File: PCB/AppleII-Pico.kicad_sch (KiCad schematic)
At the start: 29 parts, among them J1 Apple II, J2 DB15_Female_HighDensity_Mount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, J3 NOPAL, J4 Conn_02x08_Odd_Even, U1 74LCX16245, U2 74LCX16245, U5 PALCE16V8H-5JC/5, U6 Pi PICO, U7 AZ1117-3.3

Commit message: Better RPi Pico footprint
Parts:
- U6: footprint Package_DIP:DIP-40_W16.51mm_SMDSocket_LongPads -> MCU_RaspberryPi_and_Boards:RPi_Pico_SMD_TH
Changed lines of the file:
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@@
     (property "Reference" "U6" (id 0) (at 110.49 17.3482 0))
     (property "Value" "Pi PICO" (id 1) (at 110.49 19.6596 0))
-    (property "Footprint" "Package_DIP:DIP-40_W16.51mm_SMDSocket_LongPads" (id 2) (at 109.22 45.72 0)
+    (property "Footprint" "MCU_RaspberryPi_and_Boards:RPi_Pico_SMD_TH" (id 2) (at 109.22 45.72 0)
       (effects (font (size 1.27 1.27)) hide)
     )
@@
     )
     (path "/00000000-0000-0000-0000-000063a68952"
-      (reference "U6") (unit 1) (value "Pi PICO") (footprint "Package_DIP:DIP-40_W16.51mm_SMDSocket_LongPads")
+      (reference "U6") (unit 1) (value "Pi PICO") (footprint "MCU_RaspberryPi_and_Boards:RPi_Pico_SMD_TH")
     )
     (path "/00000000-0000-0000-0000-00006698c94f"

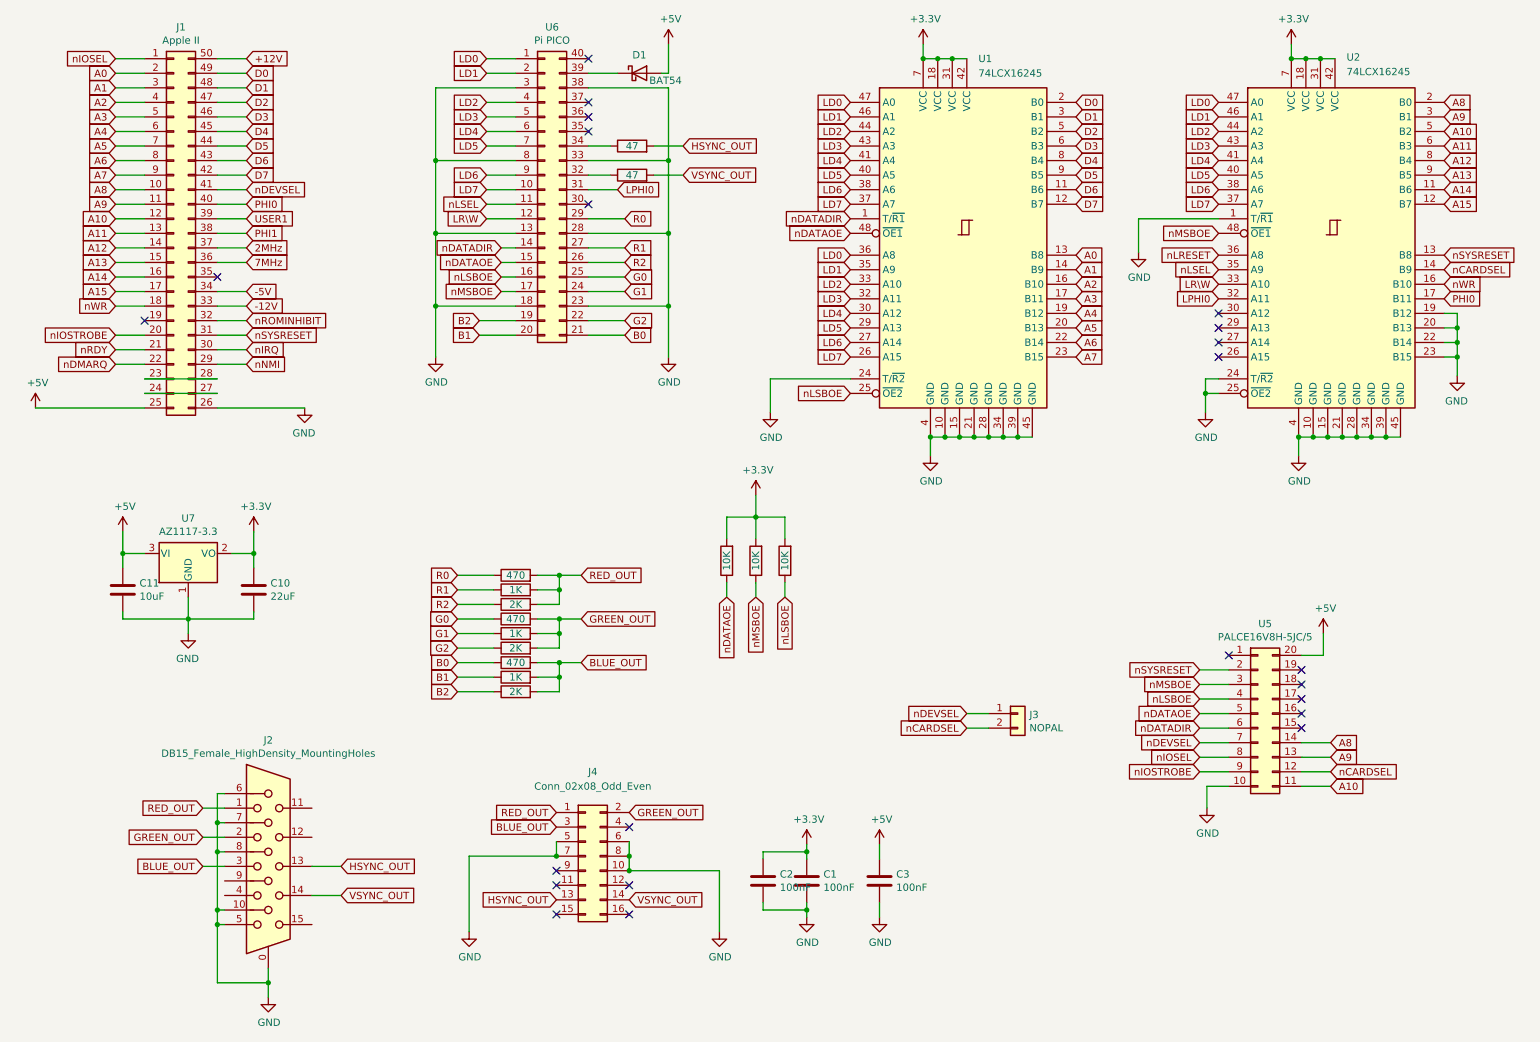
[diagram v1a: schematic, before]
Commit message: incorporate feedback
 - Pico W antenna cutout
 - Pico RUN button
 - Break-away HD15A connector
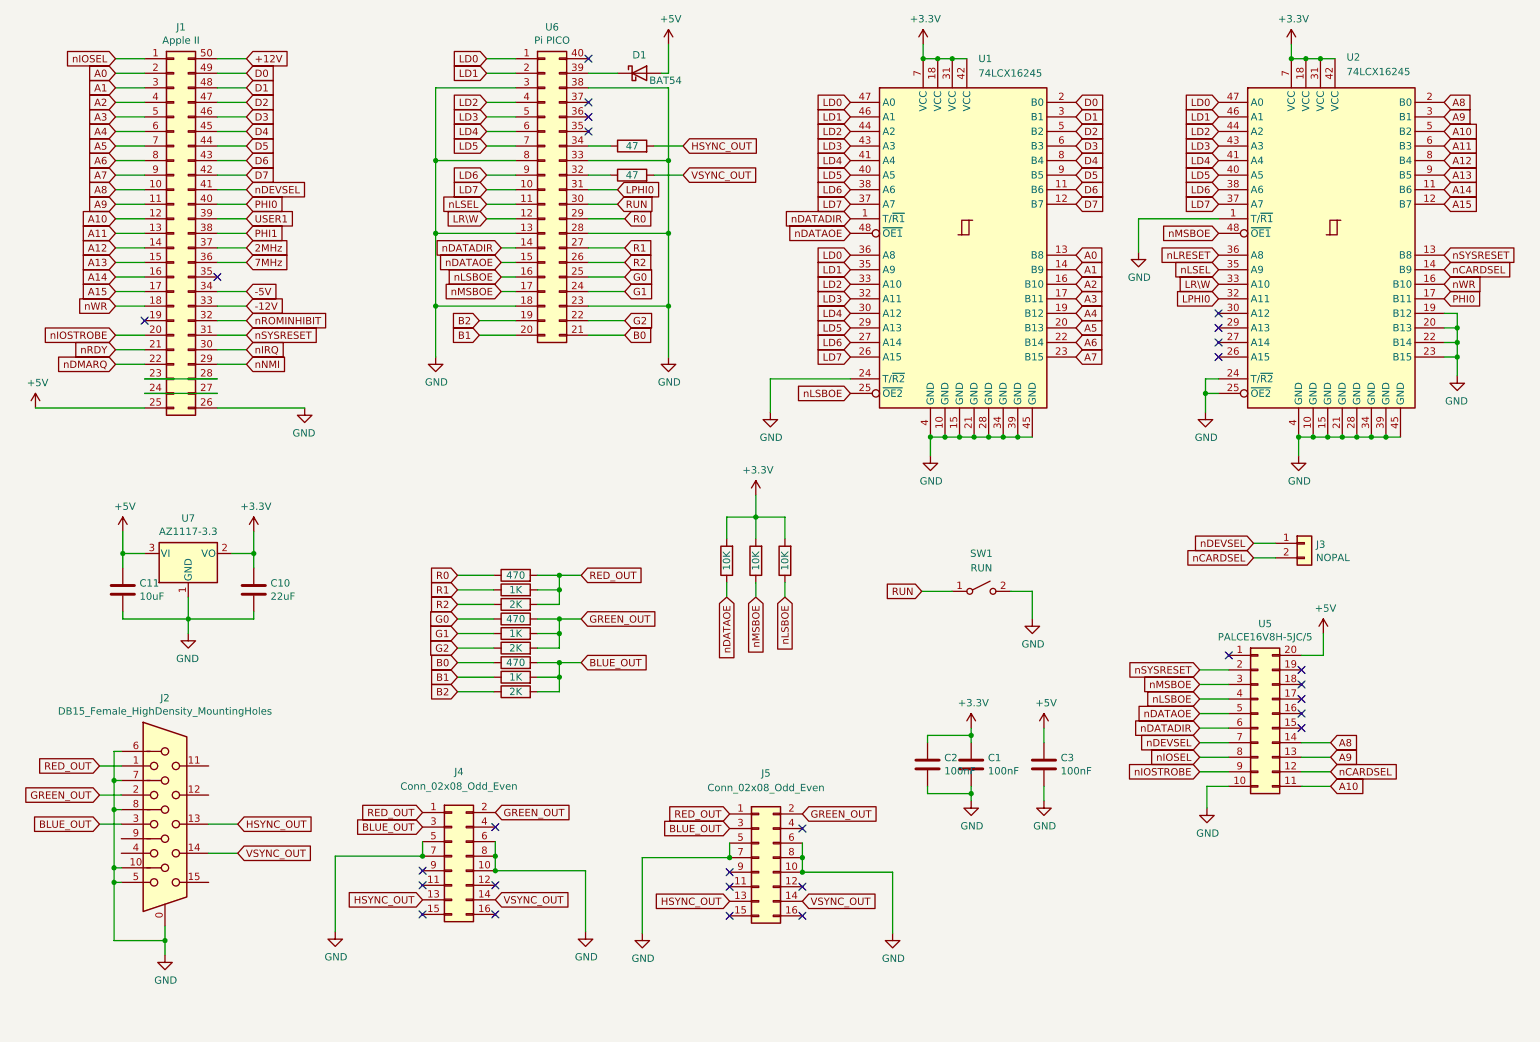
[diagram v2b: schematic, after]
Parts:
- added J5: Conn_02x08_Odd_Even, Connector_PinHeader_2.54mm:PinHeader_2x08_P2.54mm_Vertical, symbol Connector_Generic:Conn_02x08_Odd_Even
- added SW1: RUN, Button_Switch_SMD:SW_Push_1P1T_NO_6x6mm_H9.5mm, symbol Switch:SW_SPST
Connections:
- net BLUE_OUT: now also J5.3 (Pin_3)
- net GND: now also J5.10 (Pin_10), J5.5 (Pin_5), J5.6 (Pin_6), J5.7 (Pin_7), J5.8 (Pin_8), SW1.2 (B)
- net GREEN_OUT: now also J5.2 (Pin_2)
- net HSYNC_OUT: now also J5.13 (Pin_13)
- net RED_OUT: now also J5.1 (Pin_1)
- net VSYNC_OUT: now also J5.14 (Pin_14)
- net RUN: now reaches U6.30 (Pin_30)
- net RUN: now also SW1.1 (A)
- no-connect marks 23 -> 28
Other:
- moved on the sheet: C1, C2, C3, J2, J3, J4

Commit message: RUN => Pico Reset
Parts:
- SW1: value RUN -> Pico Reset
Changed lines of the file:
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@@
     (in_bom yes) (on_board yes)
     (property "Reference" "SW1" (id 0) (at 185.42 109.22 0))
-    (property "Value" "RUN" (id 1) (at 185.42 111.76 0))
+    (property "Value" "Pico Reset" (id 1) (at 185.42 111.76 0))
     (property "Footprint" "Button_Switch_SMD:SW_Push_1P1T_NO_6x6mm_H9.5mm" (id 2) (at 185.42 115.824 0)
       (effects (font (size 1.27 1.27)) hide)
@@
     )
     (path "/c1078c71-8ecb-4416-b362-632bf351b877"
-      (reference "SW1") (unit 1) (value "RUN") (footprint "Button_Switch_SMD:SW_Push_1P1T_NO_6x6mm_H9.5mm")
+      (reference "SW1") (unit 1) (value "Pico Reset") (footprint "Button_Switch_SMD:SW_Push_1P1T_NO_6x6mm_H9.5mm")
     )
     (path "/c189b8bd-871a-49df-bd93-46ab30fbe2a1"

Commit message: Fix TSSOP-48 footprint and move NOPAL
 - Use correct footprint for the TSSOP-48 case (closes #2)
 - Rename NOPAL to NOGAL and move it into the GAL footprint (closes #3)
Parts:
- J3: value NOPAL -> NOGAL
- U1: footprint Package_SO:TSSOP-48_8x12.5mm_P0.5mm -> Package_SO:TSSOP-48_6.1x9.7mm_P0.4mm
- U2: footprint Package_SO:TSSOP-48_8x12.5mm_P0.5mm -> Package_SO:TSSOP-48_6.1x12.5mm_P0.5mm
- U5: value PALCE16V8H-5JC/5 -> GAL16V8
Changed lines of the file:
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@@
     )
   )
-  (global_label "nCARDSEL" (shape input) (at 246.38 147.32 0) (fields_autoplaced)
-    (effects (font (size 1.27 1.27)) (justify left))
-    (property "Intersheet References" "${INTERSHEET_REFS}" (id 0) (at 0 0 0)
-      (effects (font (size 1.27 1.27)) hide)
+  (global_label "nCARDSEL" (shape output) (at 246.38 147.32 0) (fields_autoplaced)
+    (effects (font (size 1.27 1.27)) (justify left))
+    (property "Intersheet References" "${INTERSHEET_REFS}" (id 0) (at 258.1385 147.2406 0)
+      (effects (font (size 1.27 1.27)) (justify left) hide)
     )
   )
@@
       (effects (font (size 1.27 1.27)) (justify left))
     )
-    (property "Value" "NOPAL" (id 1) (at 243.84 109.9566 0)
+    (property "Value" "NOGAL" (id 1) (at 243.84 109.9566 0)
       (effects (font (size 1.27 1.27)) (justify left))
     )
@@
     (in_bom yes) (on_board yes)
     (property "Reference" "U5" (id 0) (at 234.95 121.4882 0))
-    (property "Value" "PALCE16V8H-5JC/5" (id 1) (at 234.95 123.7996 0))
+    (property "Value" "GAL16V8" (id 1) (at 234.95 123.7996 0))
     (property "Footprint" "Package_LCC:PLCC-20" (id 2) (at 233.68 137.16 0)
       (effects (font (size 1.27 1.27)) hide)
@@
       (effects (font (size 1.27 1.27)) (justify left))
     )
-    (property "Footprint" "Package_SO:TSSOP-48_8x12.5mm_P0.5mm" (id 2) (at 207.264 21.336 0)
+    (property "Footprint" "Package_SO:TSSOP-48_6.1x9.7mm_P0.4mm" (id 2) (at 207.264 21.336 0)
       (effects (font (size 1.27 1.27)) hide)
     )
@@
       (effects (font (size 1.27 1.27)) (justify left))
     )
-    (property "Footprint" "Package_SO:TSSOP-48_8x12.5mm_P0.5mm" (id 2) (at 271.526 21.336 0)
+    (property "Footprint" "Package_SO:TSSOP-48_6.1x12.5mm_P0.5mm" (id 2) (at 271.526 21.336 0)
       (effects (font (size 1.27 1.27)) hide)
     )
@@
     )
     (path "/00000000-0000-0000-0000-000063a3190c"
-      (reference "J3") (unit 1) (value "NOPAL") (footprint "Jumper:SolderJumper-2_P1.3mm_Open_TrianglePad1.0x1.5mm")
+      (reference "J3") (unit 1) (value "NOGAL") (footprint "Jumper:SolderJumper-2_P1.3mm_Open_TrianglePad1.0x1.5mm")
     )
     (path "/40c1df59-d376-490e-82b7-b056f34f1afc"
@@
     )
     (path "/c189b8bd-871a-49df-bd93-46ab30fbe2a1"
-      (reference "U1") (unit 1) (value "74LCX16245") (footprint "Package_SO:TSSOP-48_8x12.5mm_P0.5mm")
+      (reference "U1") (unit 1) (value "74LCX16245") (footprint "Package_SO:TSSOP-48_6.1x9.7mm_P0.4mm")
     )
     (path "/da52514b-32f6-46c0-9351-0f5bbc5d8c8f"
-      (reference "U2") (unit 1) (value "74LCX16245") (footprint "Package_SO:TSSOP-48_8x12.5mm_P0.5mm")
+      (reference "U2") (unit 1) (value "74LCX16245") (footprint "Package_SO:TSSOP-48_6.1x12.5mm_P0.5mm")
     )
     (path "/00000000-0000-0000-0000-000066540aaf"
-      (reference "U5") (unit 1) (value "PALCE16V8H-5JC/5") (footprint "Package_LCC:PLCC-20")
+      (reference "U5") (unit 1) (value "GAL16V8") (footprint "Package_LCC:PLCC-20")
     )
     (path "/00000000-0000-0000-0000-000063a68952"

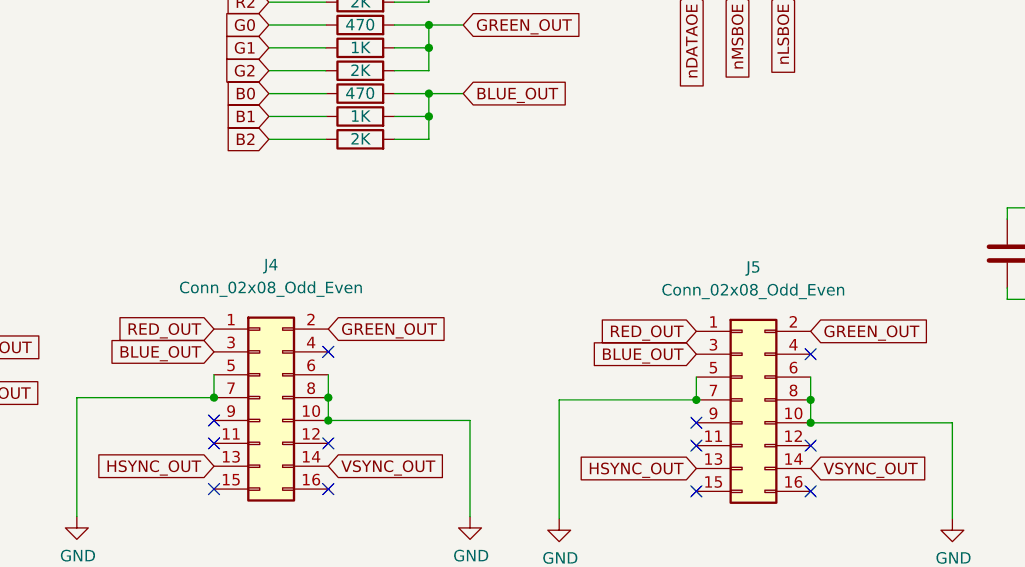
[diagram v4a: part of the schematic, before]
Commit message: silkscreen tweaks
closes #4
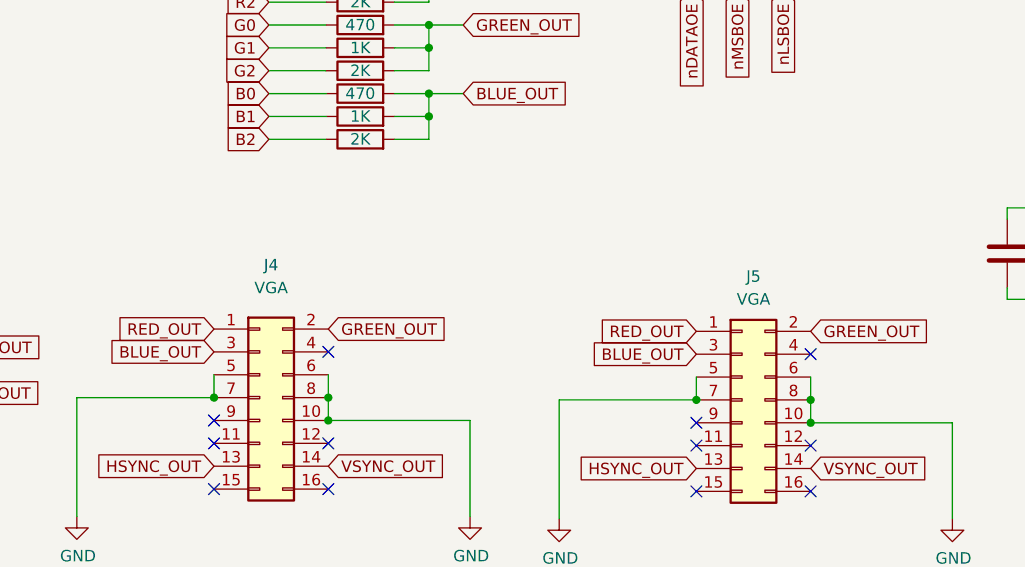
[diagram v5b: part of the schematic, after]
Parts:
- J4, J5: value Conn_02x08_Odd_Even -> VGA
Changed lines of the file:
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@@
     (in_bom yes) (on_board yes) (fields_autoplaced)
     (property "Reference" "J4" (id 0) (at 94.234 147.32 0))
-    (property "Value" "Conn_02x08_Odd_Even" (id 1) (at 94.234 149.86 0))
+    (property "Value" "VGA" (id 1) (at 94.234 149.86 0))
     (property "Footprint" "Connector_PinHeader_2.54mm:PinHeader_2x08_P2.54mm_Vertical" (id 2) (at 92.964 162.052 0)
       (effects (font (size 1.27 1.27)) hide)
@@
   (symbol (lib_id "Connector_Generic:Conn_02x08_Odd_Even") (at 146.558 162.306 0) (unit 1)
     (in_bom yes) (on_board yes) (fields_autoplaced)
-    (property "Reference" "J5" (id 0) (at 147.828 147.574 0))
-    (property "Value" "Conn_02x08_Odd_Even" (id 1) (at 147.828 150.114 0))
+    (property "Reference" "J5" (id 0) (at 147.828 148.59 0))
+    (property "Value" "VGA" (id 1) (at 147.828 151.13 0))
     (property "Footprint" "Connector_PinHeader_2.54mm:PinHeader_2x08_P2.54mm_Vertical" (id 2) (at 146.558 162.306 0)
       (effects (font (size 1.27 1.27)) hide)
@@
     )
     (path "/40c1df59-d376-490e-82b7-b056f34f1afc"
-      (reference "J4") (unit 1) (value "Conn_02x08_Odd_Even") (footprint "Connector_PinHeader_2.54mm:PinHeader_2x08_P2.54mm_Vertical")
+      (reference "J4") (unit 1) (value "VGA") (footprint "Connector_PinHeader_2.54mm:PinHeader_2x08_P2.54mm_Vertical")
     )
     (path "/9e580525-7ff5-402d-ba03-5fb3f2ecc0b7"
-      (reference "J5") (unit 1) (value "Conn_02x08_Odd_Even") (footprint "Connector_PinHeader_2.54mm:PinHeader_2x08_P2.54mm_Vertical")
+      (reference "J5") (unit 1) (value "VGA") (footprint "Connector_PinHeader_2.54mm:PinHeader_2x08_P2.54mm_Vertical")
     )
     (path "/00000000-0000-0000-0000-000064ae92cf"

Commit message: Add BOM and production files
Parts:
- C1, C2, C3: LCSC (none) -> C2857981
- C10: LCSC (none) -> C5181863
- C11: LCSC (none) -> C123608
- D1: LCSC (none) -> C5204731
- R1, R4, R7: LCSC (none) -> C5140094
- R10, R11: LCSC (none) -> C3016437
- R12, R13, R14: LCSC (none) -> C3017715
- R2, R5, R8: LCSC (none) -> C3016283
- R3, R6, R9: LCSC (none) -> C3016472
- SW1: LCSC (none) -> C5381239
- U1, U2: LCSC (none) -> C894789
- U7: LCSC (none) -> C110474
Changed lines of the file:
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@@
+      (effects (font (size 1.27 1.27)) hide)
+    )
+    (property "LCSC" "C3017715" (at 146.05 110.49 90)
       (effects (font (size 1.27 1.27)) hide)
     )
@@
       (effects (font (size 1.27 1.27)) hide)
     )
+    (property "LCSC" "C3017715" (at 151.13 110.49 90)
+      (effects (font (size 1.27 1.27)) hide)
+    )
     (pin "1")
     (pin "2")
@@
       (effects (font (size 1.27 1.27)) hide)
     )
+    (property "LCSC" "C3017715" (at 140.97 110.49 90)
+      (effects (font (size 1.27 1.27)) hide)
+    )
     (pin "1")
     (pin "2")
@@
       (effects (font (size 1.27 1.27)) hide)
     )
+    (property "LCSC" "C3016472" (at 104.14 133.35 90)
+      (effects (font (size 1.27 1.27)) hide)
+    )
     (pin "1")
     (pin "2")
@@
       (effects (font (size 1.27 1.27)) hide)
     )
+    (property "LCSC" "C2857981" (at 176.022 146.05 0)
+      (effects (font (size 1.27 1.27)) hide)
+    )
     (pin "1")
     (pin "2")
@@
     )
     (property "Datasheet" "~" (at 183.642 146.05 0)
+      (effects (font (size 1.27 1.27)) hide)
+    )
+    (property "LCSC" "C2857981" (at 183.642 146.05 0)
       (effects (font (size 1.27 1.27)) hide)
     )
@@
       (effects (font (size 1.27 1.27)) hide)
     )
+    (property "LCSC" "C5204731" (at 125.73 25.4 0)
+      (effects (font (size 1.27 1.27)) hide)
+    )
     (pin "1")
     (pin "2")
@@
       (effects (font (size 1.27 1.27)) hide)
     )
+    (property "LCSC" "C3016437" (at 124.46 38.1 90)
+      (effects (font (size 1.27 1.27)) hide)
+    )
     (pin "1")
     (pin "2")
@@
       (effects (font (size 1.27 1.27)) hide)
     )
+    (property "LCSC" "C3016437" (at 124.46 43.18 90)
+      (effects (font (size 1.27 1.27)) hide)
+    )
     (pin "1")
     (pin "2")
@@
       (effects (font (size 1.27 1.27)) hide)
     )
+    (property "LCSC" "C3016283" (at 104.14 130.81 90)
+      (effects (font (size 1.27 1.27)) hide)
+    )
     (pin "1")
     (pin "2")
@@
       (effects (font (size 1.27 1.27)) hide)
     )
+    (property "LCSC" "C5140094" (at 104.14 128.27 90)
+      (effects (font (size 1.27 1.27)) hide)
+    )
     (pin "1")
     (pin "2")
@@
       (effects (font (size 1.27 1.27)) hide)
     )
+    (property "LCSC" "C3016472" (at 104.14 125.73 90)
+      (effects (font (size 1.27 1.27)) hide)
+    )
     (pin "1")
     (pin "2")
@@
       (effects (font (size 1.27 1.27)) hide)
     )
+    (property "LCSC" "C3016283" (at 104.14 123.19 90)
+      (effects (font (size 1.27 1.27)) hide)
+    )
     (pin "1")
     (pin "2")
@@
       (effects (font (size 1.27 1.27)) hide)
     )
+    (property "LCSC" "C5140094" (at 104.14 120.65 90)
+      (effects (font (size 1.27 1.27)) hide)
+    )
     (pin "1")
     (pin "2")
@@
       (effects (font (size 1.27 1.27)) hide)
     )
+    (property "LCSC" "C3016472" (at 104.14 118.11 90)
+      (effects (font (size 1.27 1.27)) hide)
+    )
     (pin "1")
     (pin "2")
@@
       (effects (font (size 1.27 1.27)) hide)
     )
+    (property "LCSC" "C3016283" (at 104.14 115.57 90)
+      (effects (font (size 1.27 1.27)) hide)
+    )
     (pin "1")
     (pin "2")
@@
     )
     (property "Datasheet" "~" (at 104.14 113.03 0)
+      (effects (font (size 1.27 1.27)) hide)
+    )
+    (property "LCSC" "C5140094" (at 104.14 113.03 90)
       (effects (font (size 1.27 1.27)) hide)
     )
@@
       (effects (font (size 1.27 1.27)) hide)
     )
+    (property "LCSC" "C110474" (at 46.99 109.22 0)
+      (effects (font (size 1.27 1.27)) hide)
+    )
     (pin "1")
     (pin "2")
@@
       (effects (font (size 1.27 1.27)) hide)
     )
+    (property "LCSC" "C123608" (at 35.56 115.57 0)
+      (effects (font (size 1.27 1.27)) hide)
+    )
     (pin "1")
     (pin "2")
@@
     )
     (property "Datasheet" "~" (at 58.42 115.57 0)
+      (effects (font (size 1.27 1.27)) hide)
+    )
+    (property "LCSC" "C5181863" (at 58.42 115.57 0)
       (effects (font (size 1.27 1.27)) hide)
     )
@@
       (effects (font (size 1.27 1.27)) hide)
     )
+    (property "LCSC" "C2857981" (at 196.342 146.05 0)
+      (effects (font (size 1.27 1.27)) hide)
+    )
     (pin "1")
     (pin "2")
@@
       (effects (font (size 1.27 1.27)) hide)
     )
+    (property "LCSC" "C5381239" (at 185.42 115.824 0)
+      (effects (font (size 1.27 1.27)) hide)
+    )
     (pin "1")
     (pin "2")
@@
     )
     (property "Datasheet" "" (at 207.264 21.336 0)
+      (effects (font (size 1.27 1.27)) hide)
+    )
+    (property "LCSC" "C894789" (at 180.34 52.07 0)
       (effects (font (size 1.27 1.27)) hide)
     )
@@
       (effects (font (size 1.27 1.27)) hide)
     )
+    (property "LCSC" "C894789" (at 244.602 52.07 0)
+      (effects (font (size 1.27 1.27)) hide)
+    )
